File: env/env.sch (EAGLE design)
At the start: 70 parts, among them IC1 DG403DJD, IC2 OPA4130U, IC3 4001D, IC4 OPA2134D, IC5 OPA4130U, Q1 BC847ALT1SMD, Q2 BC857ALT1SMD, X1 2516-

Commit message: worked on the env some more
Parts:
- added EOF, EOR: PJ301BM, dan:PJ301BM
- added R45: 1k, dan:R-US_R0603
- R25: value 10k -> 1k
- R28: value US-EVUF3J -> 1k; device dan:US-EVUF3J -> dan:R-US_R0603
- renumbered AUV1 to OS
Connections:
- removed net N$43: ACVA.S
- new net N$47: EOR.P$3, R28.1
- new net N$49: EOF.P$3, R45.1
- new net N$50: ACVA.S, R20.2
- net ASCV: now also R19.2
- net GND: now also CVOUT.P$1, CVOUT.P$2, CVOUT.P$4, EOF.P$1, EOF.P$2, EOF.P$4, EOR.P$1, EOR.P$2, EOR.P$4, GATE.P$1, GATE.P$2, GATE.P$4
- net N$2: now also R28.2
- net N$25: no longer R28.E
- net N$29: no longer R28.A
- net N$31: no longer R28.S
- net N$9: now also R45.2
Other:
- note added: "Is this right?"
- moved on the sheet: R20

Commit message: more work on the env.
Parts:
- added C10, C11, C12, C13, C14, C5, C6, C7, C8, C9: 1u, dan:C-USC0603
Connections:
- net +12V: now also C5.1, C6.1, C7.1, C8.1, C9.1
- net -12V: now also C10.1, C11.1, C12.1, C13.1, C14.1
- net GND: now also C10.2, C11.2, C12.2, C13.2, C14.2, C5.2, C6.2, C7.2, C8.2, C9.2
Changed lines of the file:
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@@
 <part name="GND23" library="dan" deviceset="GND" device=""/>
 <part name="GND24" library="dan" deviceset="GND" device=""/>
+<part name="C5" library="dan" deviceset="C-US" device="C0603" value="1u"/>
+<part name="C6" library="dan" deviceset="C-US" device="C0603" value="1u"/>
+<part name="C7" library="dan" deviceset="C-US" device="C0603" value="1u"/>
+<part name="C8" library="dan" deviceset="C-US" device="C0603" value="1u"/>
+<part name="C9" library="dan" deviceset="C-US" device="C0603" value="1u"/>
+<part name="C10" library="dan" deviceset="C-US" device="C0603" value="1u"/>
+<part name="C11" library="dan" deviceset="C-US" device="C0603" value="1u"/>
+<part name="C12" library="dan" deviceset="C-US" device="C0603" value="1u"/>
+<part name="C13" library="dan" deviceset="C-US" device="C0603" value="1u"/>
+<part name="C14" library="dan" deviceset="C-US" device="C0603" value="1u"/>
+<part name="P+12" library="dan" deviceset="+12V" device=""/>
+<part name="P-9" library="dan" deviceset="-12V" device=""/>
+<part name="GND25" library="dan" deviceset="GND" device=""/>
 </parts>
 <sheets>
@@
 <instance part="GND23" gate="1" x="170.18" y="132.08"/>
 <instance part="GND24" gate="1" x="228.6" y="53.34"/>
+<instance part="C5" gate="G$1" x="-88.9" y="43.18"/>
+<instance part="C6" gate="G$1" x="-81.28" y="43.18"/>
+<instance part="C7" gate="G$1" x="-73.66" y="43.18"/>
+<instance part="C8" gate="G$1" x="-66.04" y="43.18"/>
+<instance part="C9" gate="G$1" x="-58.42" y="43.18"/>
+<instance part="C10" gate="G$1" x="-88.9" y="27.94" rot="R180"/>
+<instance part="C11" gate="G$1" x="-81.28" y="27.94" rot="R180"/>
+<instance part="C12" gate="G$1" x="-73.66" y="27.94" rot="R180"/>
+<instance part="C13" gate="G$1" x="-66.04" y="27.94" rot="R180"/>
+<instance part="C14" gate="G$1" x="-58.42" y="27.94" rot="R180"/>
+<instance part="P+12" gate="1" x="-68.58" y="53.34"/>
+<instance part="P-9" gate="1" x="-73.66" y="17.78"/>
+<instance part="GND25" gate="1" x="-48.26" y="30.48"/>
 </instances>
 <busses>
@@
 <junction x="175.26" y="139.7"/>
 </segment>
+<segment>
+<pinref part="GND25" gate="1" pin="GND"/>
+<wire x1="-48.26" y1="33.02" x2="-48.26" y2="35.56" width="0.1524" layer="91"/>
+<pinref part="C10" gate="G$1" pin="2"/>
+<wire x1="-48.26" y1="35.56" x2="-58.42" y2="35.56" width="0.1524" layer="91"/>
+<wire x1="-58.42" y1="35.56" x2="-66.04" y2="35.56" width="0.1524" layer="91"/>
+<wire x1="-66.04" y1="35.56" x2="-73.66" y2="35.56" width="0.1524" layer="91"/>
+<wire x1="-73.66" y1="35.56" x2="-81.28" y2="35.56" width="0.1524" layer="91"/>
+<wire x1="-81.28" y1="35.56" x2="-88.9" y2="35.56" width="0.1524" layer="91"/>
+<wire x1="-88.9" y1="35.56" x2="-88.9" y2="33.02" width="0.1524" layer="91"/>
+<pinref part="C5" gate="G$1" pin="2"/>
+<wire x1="-88.9" y1="38.1" x2="-88.9" y2="35.56" width="0.1524" layer="91"/>
+<pinref part="C6" gate="G$1" pin="2"/>
+<wire x1="-81.28" y1="38.1" x2="-81.28" y2="35.56" width="0.1524" layer="91"/>
+<pinref part="C7" gate="G$1" pin="2"/>
+<wire x1="-73.66" y1="38.1" x2="-73.66" y2="35.56" width="0.1524" layer="91"/>
+<pinref part="C8" gate="G$1" pin="2"/>
+<wire x1="-66.04" y1="38.1" x2="-66.04" y2="35.56" width="0.1524" layer="91"/>
+<pinref part="C9" gate="G$1" pin="2"/>
+<wire x1="-58.42" y1="38.1" x2="-58.42" y2="35.56" width="0.1524" layer="91"/>
+<pinref part="C14" gate="G$1" pin="2"/>
+<wire x1="-58.42" y1="33.02" x2="-58.42" y2="35.56" width="0.1524" layer="91"/>
+<pinref part="C13" gate="G$1" pin="2"/>
+<wire x1="-66.04" y1="33.02" x2="-66.04" y2="35.56" width="0.1524" layer="91"/>
+<pinref part="C12" gate="G$1" pin="2"/>
+<wire x1="-73.66" y1="33.02" x2="-73.66" y2="35.56" width="0.1524" layer="91"/>
+<pinref part="C11" gate="G$1" pin="2"/>
+<wire x1="-81.28" y1="33.02" x2="-81.28" y2="35.56" width="0.1524" layer="91"/>
+<junction x="-88.9" y="35.56"/>
+<junction x="-81.28" y="35.56"/>
+<junction x="-73.66" y="35.56"/>
+<junction x="-66.04" y="35.56"/>
+<junction x="-58.42" y="35.56"/>
+</segment>
 </net>
 <net name="N$3" class="0">
@@
 <junction x="-76.2" y="101.6"/>
 </segment>
+<segment>
+<pinref part="C5" gate="G$1" pin="1"/>
+<wire x1="-88.9" y1="45.72" x2="-88.9" y2="48.26" width="0.1524" layer="91"/>
+<pinref part="C9" gate="G$1" pin="1"/>
+<wire x1="-88.9" y1="48.26" x2="-81.28" y2="48.26" width="0.1524" layer="91"/>
+<wire x1="-81.28" y1="48.26" x2="-73.66" y2="48.26" width="0.1524" layer="91"/>
+<wire x1="-73.66" y1="48.26" x2="-68.58" y2="48.26" width="0.1524" layer="91"/>
+<wire x1="-68.58" y1="48.26" x2="-66.04" y2="48.26" width="0.1524" layer="91"/>
+<wire x1="-66.04" y1="48.26" x2="-58.42" y2="48.26" width="0.1524" layer="91"/>
+<wire x1="-58.42" y1="48.26" x2="-58.42" y2="45.72" width="0.1524" layer="91"/>
+<pinref part="C8" gate="G$1" pin="1"/>
+<wire x1="-66.04" y1="45.72" x2="-66.04" y2="48.26" width="0.1524" layer="91"/>
+<pinref part="C7" gate="G$1" pin="1"/>
+<wire x1="-73.66" y1="45.72" x2="-73.66" y2="48.26" width="0.1524" layer="91"/>
+<pinref part="C6" gate="G$1" pin="1"/>
+<wire x1="-81.28" y1="45.72" x2="-81.28" y2="48.26" width="0.1524" layer="91"/>
+<pinref part="P+12" gate="1" pin="+12V"/>
+<wire x1="-68.58" y1="50.8" x2="-68.58" y2="48.26" width="0.1524" layer="91"/>
+<junction x="-66.04" y="48.26"/>
+<junction x="-73.66" y="48.26"/>
+<junction x="-81.28" y="48.26"/>
+</segment>
 </net>
 <net name="-12V" class="0">
@@
 <junction x="-76.2" y="124.46"/>
 </segment>
-</net>
+<segment>
+<pinref part="C10" gate="G$1" pin="1"/>
+<wire x1="-88.9" y1="25.4" x2="-88.9" y2="22.86" width="0.1524" layer="91"/>
+<pinref part="C14" gate="G$1" pin="1"/>
+<wire x1="-88.9" y1="22.86" x2="-81.28" y2="22.86" width="0.1524" layer="91"/>
+<wire x1="-81.28" y1="22.86" x2="-73.66" y2="22.86" width="0.1524" layer="91"/>
+<wire x1="-73.66" y1="22.86" x2="-66.04" y2="22.86" width="0.1524" layer="91"/>
+<wire x1="-66.04" y1="22.86" x2="-58.42" y2="22.86" width="0.1524" layer="91"/>
+<wire x1="-58.42" y1="22.86" x2="-58.42" y2="25.4" width="0.1524" layer="91"/>
+<pinref part="C13" gate="G$1" pin="1"/>
+<wire x1="-66.04" y1="25.4" x2="-66.04" y2="22.86" width="0.1524" layer="91"/>
+<pinref part="C12" gate="G$1" pin="1"/>
+<wire x1="-73.66" y1="25.4" x2="-73.66" y2="22.86" width="0.1524" layer="91"/>
+<pinref part="C11" gate="G$1" pin="1"/>
+<wire x1="-81.28" y1="25.4" x2="-81.28" y2="22.86" width="0.1524" layer="91"/>
+<pinref part="P-9" gate="1" pin="-12V"/>
+<wire x1="-73.66" y1="20.32" x2="-73.66" y2="22.86" width="0.1524" layer="91"/>
+<junction x="-73.66" y="22.86"/>
+<junction x="-66.04" y="22.86"/>
+<junction x="-81.28" y="22.86"/>
+</segment>
+</net>

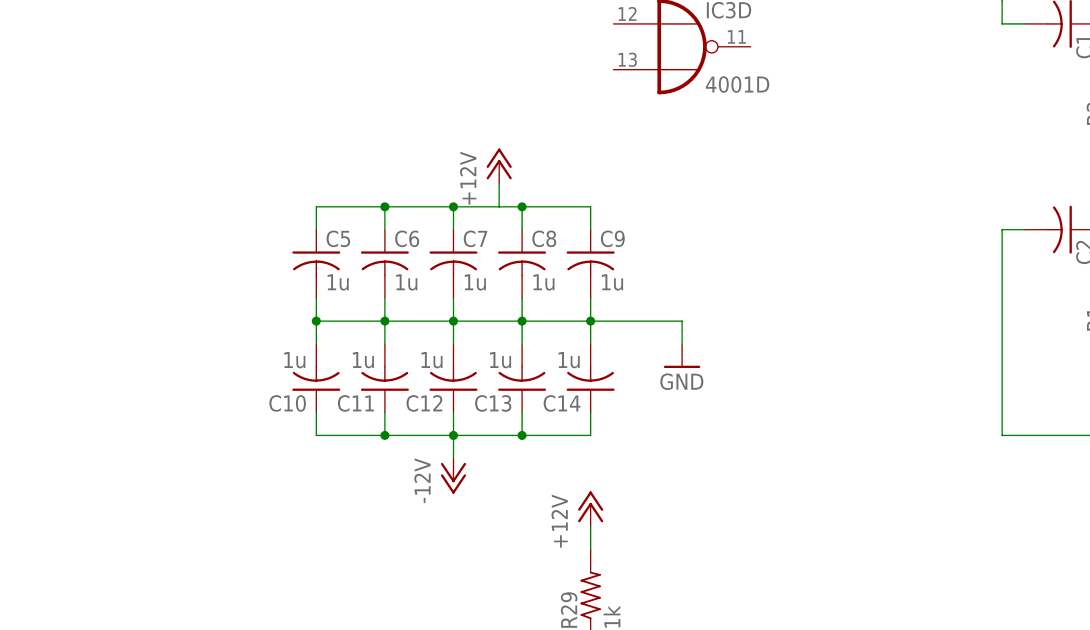
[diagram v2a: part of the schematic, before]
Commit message: almost done with the env.  need to check things (pot polarity)
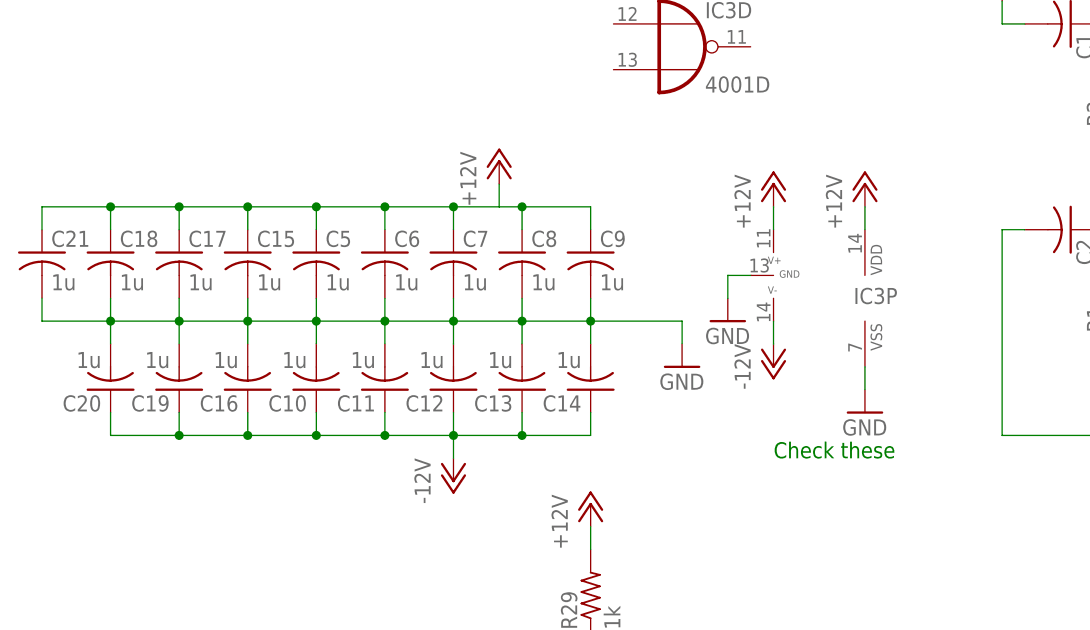
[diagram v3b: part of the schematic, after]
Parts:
- added C15, C16, C17, C18, C19, C20, C21: 1u, dan:C-USC0603
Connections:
- net +12V: now also C15.1, C17.1, C18.1, C21.1, IC1P.V+, IC3P.VDD
- net -12V: now also C16.1, C19.1, C20.1, IC1P.V-
- net GND: now also C15.2, C16.2, C17.2, C18.2, C19.2, C20.2, C21.2, IC1P.GND, IC3P.VSS
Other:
- note added: "Check these"
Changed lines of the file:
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@@
 <part name="P-9" library="dan" deviceset="-12V" device=""/>
 <part name="GND25" library="dan" deviceset="GND" device=""/>
+<part name="P+13" library="dan" deviceset="+12V" device=""/>
+<part name="P-11" library="dan" deviceset="-12V" device=""/>
+<part name="P+14" library="dan" deviceset="+12V" device=""/>
+<part name="GND26" library="dan" deviceset="GND" device=""/>
+<part name="GND27" library="dan" deviceset="GND" device=""/>
+<part name="C15" library="dan" deviceset="C-US" device="C0603" value="1u"/>
+<part name="C16" library="dan" deviceset="C-US" device="C0603" value="1u"/>
+<part name="C17" library="dan" deviceset="C-US" device="C0603" value="1u"/>
+<part name="C18" library="dan" deviceset="C-US" device="C0603" value="1u"/>
+<part name="C19" library="dan" deviceset="C-US" device="C0603" value="1u"/>
+<part name="C20" library="dan" deviceset="C-US" device="C0603" value="1u"/>
+<part name="C21" library="dan" deviceset="C-US" device="C0603" value="1u"/>
 </parts>
 <sheets>
@@
 <text x="5.08" y="-53.34" size="1.778" layer="91">Is this right?</text>
 <text x="101.6" y="76.2" size="1.778" layer="91">Is this right?</text>
+<text x="-38.1" y="20.32" size="1.778" layer="91">Check these</text>
 </plain>
 <instances>
@@
 <instance part="P-9" gate="1" x="-73.66" y="17.78"/>
 <instance part="GND25" gate="1" x="-48.26" y="30.48"/>
+<instance part="IC3" gate="P" x="-27.94" y="38.1"/>
+<instance part="P+13" gate="1" x="-27.94" y="50.8"/>
+<instance part="IC1" gate="P" x="-38.1" y="40.64"/>
+<instance part="P-11" gate="1" x="-38.1" y="30.48"/>
+<instance part="P+14" gate="1" x="-38.1" y="50.8"/>
+<instance part="GND26" gate="1" x="-43.18" y="35.56"/>
+<instance part="GND27" gate="1" x="-27.94" y="25.4"/>
+<instance part="C15" gate="G$1" x="-96.52" y="43.18"/>
+<instance part="C16" gate="G$1" x="-96.52" y="27.94" rot="R180"/>
+<instance part="C17" gate="G$1" x="-104.14" y="43.18"/>
+<instance part="C18" gate="G$1" x="-111.76" y="43.18"/>
+<instance part="C19" gate="G$1" x="-104.14" y="27.94" rot="R180"/>
+<instance part="C20" gate="G$1" x="-111.76" y="27.94" rot="R180"/>
+<instance part="C21" gate="G$1" x="-119.38" y="43.18"/>
 </instances>
 <busses>
@@
 <junction x="-66.04" y="35.56"/>
 <junction x="-58.42" y="35.56"/>
+<pinref part="C15" gate="G$1" pin="2"/>
+<wire x1="-88.9" y1="35.56" x2="-96.52" y2="35.56" width="0.1524" layer="91"/>
+<wire x1="-96.52" y1="35.56" x2="-96.52" y2="38.1" width="0.1524" layer="91"/>
+<pinref part="C16" gate="G$1" pin="2"/>
+<wire x1="-96.52" y1="33.02" x2="-96.52" y2="35.56" width="0.1524" layer="91"/>
+<pinref part="C17" gate="G$1" pin="2"/>
+<wire x1="-104.14" y1="38.1" x2="-104.14" y2="35.56" width="0.1524" layer="91"/>
+<wire x1="-104.14" y1="35.56" x2="-96.52" y2="35.56" width="0.1524" layer="91"/>
+<junction x="-96.52" y="35.56"/>
+<pinref part="C19" gate="G$1" pin="2"/>
+<wire x1="-104.14" y1="33.02" x2="-104.14" y2="35.56" width="0.1524" layer="91"/>
+<pinref part="C18" gate="G$1" pin="2"/>
+<wire x1="-104.14" y1="35.56" x2="-111.76" y2="35.56" width="0.1524" layer="91"/>
+<wire x1="-111.76" y1="35.56" x2="-111.76" y2="38.1" width="0.1524" layer="91"/>
+<junction x="-104.14" y="35.56"/>
+<pinref part="C21" gate="G$1" pin="2"/>
+<wire x1="-119.38" y1="38.1" x2="-119.38" y2="35.56" width="0.1524" layer="91"/>
+<wire x1="-119.38" y1="35.56" x2="-111.76" y2="35.56" width="0.1524" layer="91"/>
+<pinref part="C20" gate="G$1" pin="2"/>
+<wire x1="-111.76" y1="33.02" x2="-111.76" y2="35.56" width="0.1524" layer="91"/>
+<junction x="-111.76" y="35.56"/>
+</segment>
+<segment>
+<pinref part="IC1" gate="P" pin="GND"/>
+<wire x1="-40.64" y1="40.64" x2="-43.18" y2="40.64" width="0.1524" layer="91"/>
+<pinref part="GND26" gate="1" pin="GND"/>
+<wire x1="-43.18" y1="40.64" x2="-43.18" y2="38.1" width="0.1524" layer="91"/>
+</segment>
+<segment>
+<pinref part="IC3" gate="P" pin="VSS"/>
+<pinref part="GND27" gate="1" pin="GND"/>
+<wire x1="-27.94" y1="27.94" x2="-27.94" y2="30.48" width="0.1524" layer="91"/>
 </segment>
 </net>
@@
 <junction x="-73.66" y="48.26"/>
 <junction x="-81.28" y="48.26"/>
+<pinref part="C15" gate="G$1" pin="1"/>
+<wire x1="-96.52" y1="45.72" x2="-96.52" y2="48.26" width="0.1524" layer="91"/>
+<wire x1="-96.52" y1="48.26" x2="-88.9" y2="48.26" width="0.1524" layer="91"/>
+<pinref part="C17" gate="G$1" pin="1"/>
+<wire x1="-104.14" y1="45.72" x2="-104.14" y2="48.26" width="0.1524" layer="91"/>
+<wire x1="-104.14" y1="48.26" x2="-96.52" y2="48.26" width="0.1524" layer="91"/>
+<junction x="-88.9" y="48.26"/>
+<junction x="-96.52" y="48.26"/>
+<pinref part="C18" gate="G$1" pin="1"/>
+<wire x1="-111.76" y1="45.72" x2="-111.76" y2="48.26" width="0.1524" layer="91"/>
+<wire x1="-111.76" y1="48.26" x2="-104.14" y2="48.26" width="0.1524" layer="91"/>
+<junction x="-104.14" y="48.26"/>
+<pinref part="C21" gate="G$1" pin="1"/>
+<wire x1="-119.38" y1="45.72" x2="-119.38" y2="48.26" width="0.1524" layer="91"/>
+<wire x1="-119.38" y1="48.26" x2="-111.76" y2="48.26" width="0.1524" layer="91"/>
+<junction x="-111.76" y="48.26"/>
+</segment>
+<segment>
+<pinref part="IC3" gate="P" pin="VDD"/>
+<pinref part="P+13" gate="1" pin="+12V"/>
+<wire x1="-27.94" y1="45.72" x2="-27.94" y2="48.26" width="0.1524" layer="91"/>
+</segment>
+<segment>
+<pinref part="IC1" gate="P" pin="V+"/>
+<pinref part="P+14" gate="1" pin="+12V"/>
+<wire x1="-38.1" y1="45.72" x2="-38.1" y2="48.26" width="0.1524" layer="91"/>
 </segment>
 </net>
@@
 <junction x="-66.04" y="22.86"/>
 <junction x="-81.28" y="22.86"/>
-</segment>
-</net>
+<pinref part="C16" gate="G$1" pin="1"/>
+<wire x1="-96.52" y1="25.4" x2="-96.52" y2="22.86" width="0.1524" layer="91"/>
+<wire x1="-96.52" y1="22.86" x2="-88.9" y2="22.86" width="0.1524" layer="91"/>
+<junction x="-88.9" y="22.86"/>
+<pinref part="C19" gate="G$1" pin="1"/>
+<wire x1="-104.14" y1="25.4" x2="-104.14" y2="22.86" width="0.1524" layer="91"/>
+<wire x1="-104.14" y1="22.86" x2="-96.52" y2="22.86" width="0.1524" layer="91"/>
+<pinref part="C20" gate="G$1" pin="1"/>
+<wire x1="-111.76" y1="25.4" x2="-111.76" y2="22.86" width="0.1524" layer="91"/>
+<wire x1="-111.76" y1="22.86" x2="-104.14" y2="22.86" width="0.1524" layer="91"/>
+<junction x="-96.52" y="22.86"/>
+<junction x="-104.14" y="22.86"/>
+</segment>
+<segment>
+<pinref part="P-11" gate="1" pin="-12V"/>
+<pinref part="IC1" gate="P" pin="V-"/>
+<wire x1="-38.1" y1="33.02" x2="-38.1" y2="35.56" width="0.1524" layer="91"/>
+</segment>
+</net>

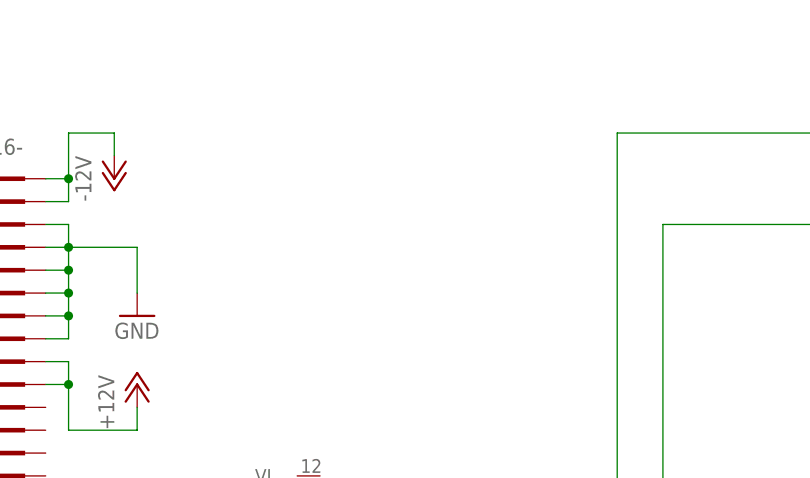
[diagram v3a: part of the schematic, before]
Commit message: added a vca.  made changes to the filter components
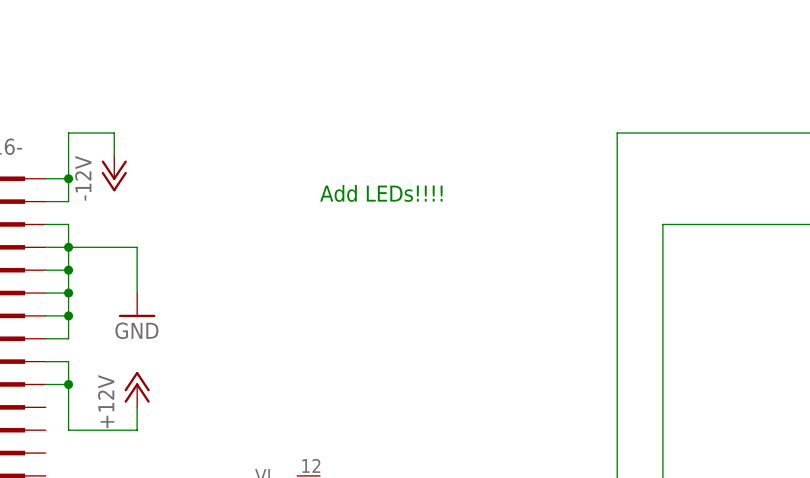
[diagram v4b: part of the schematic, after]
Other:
- note added: "Add LEDs!!!!"
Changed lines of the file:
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@@
 <text x="101.6" y="76.2" size="1.778" layer="91">Is this right?</text>
 <text x="-38.1" y="20.32" size="1.778" layer="91">Check these</text>
+<text x="-48.26" y="121.92" size="1.778" layer="91">Add LEDs!!!!</text>
 </plain>
 <instances>
